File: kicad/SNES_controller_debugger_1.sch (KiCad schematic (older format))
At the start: 28 parts, among them J1 ICSP, J2 CONTROLLER_OUT, J3 MICRO_USB, Q1 DMG2302UK-7, Q2 DMP2215L-7, SW1 Reset_switch, U1 ATmega32U4, Y1 16MHz

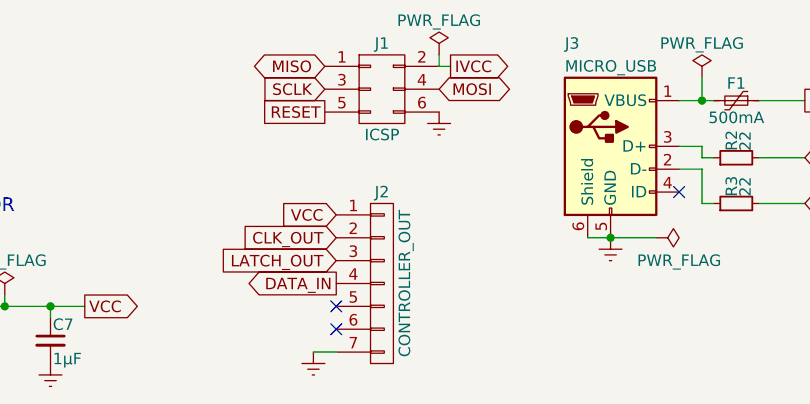
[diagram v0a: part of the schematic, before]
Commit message: pcb: Fix/add some footprints
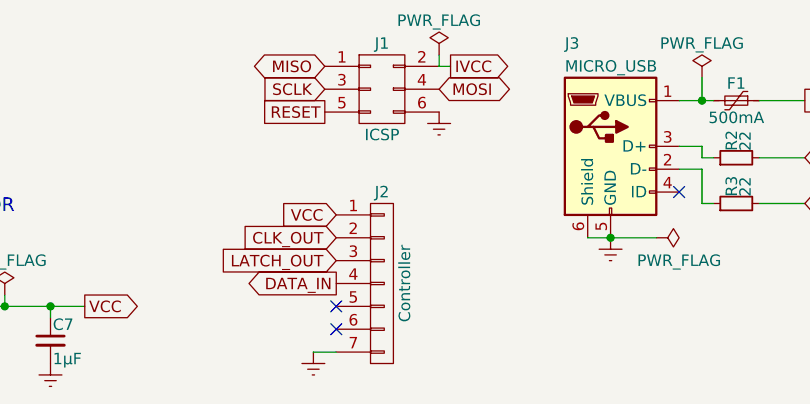
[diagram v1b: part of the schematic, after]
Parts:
- J2: value CONTROLLER_OUT -> Controller
- SW1: value Reset_switch -> Reset
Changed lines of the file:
@@
 LIBS:ftdi
 LIBS:gennum
-LIBS:graphic
 LIBS:hc11
 LIBS:ir
 LIBS:Lattice
 LIBS:leds
-LIBS:logo
 LIBS:maxim
 LIBS:mechanical
@@
 P 6200 5650
 F 0 "J2" H 6200 6050 50  0000 C CNN
-F 1 "CONTROLLER_OUT" V 6300 5650 50  0000 C CNN
+F 1 "Controller" V 6300 5650 50  0000 C CNN
 F 2 "SNES_Controller_Port:SNES_controller_port" H 6200 5650 50  0001 C CNN
 F 3 "" H 6200 5650 50  0001 C CNN
@@
 P 1050 3300
 F 0 "SW1" H 1100 3400 50  0000 L CNN
-F 1 "Reset_switch" H 1050 3240 50  0001 C CNN
+F 1 "Reset" H 1050 3240 50  0001 C CNN
 F 2 "Buttons_Switches_THT:SW_PUSH_6mm" H 1050 3500 50  0001 C CNN
 F 3 "" H 1050 3500 50  0001 C CNN
